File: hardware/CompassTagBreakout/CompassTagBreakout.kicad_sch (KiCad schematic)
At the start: 15 parts, among them J3 Conn_01x17, J4 Conn_01x17, U1 TPS7A2018PDQN, U2 AT25XE321, U3 AK09940A, U4 LIS2DU12TR

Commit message: checkpoint
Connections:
- net AK_MISO: now also U3.B4 (SO); no longer U3.A4 (SDA/SI)
- net AK_MOSI: now also U3.A4 (SDA/SI); no longer U3.B4 (SO)
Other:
- title: Tag Breakout Board Steval Dauguter -> Compass Tag Breakout
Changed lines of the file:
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@@
 	(paper "A")
 	(title_block
-		(title "Tag Breakout Board Steval Dauguter")
-		(date "2020-10-24")
+		(title "Compass Tag Breakout")
+		(date "2025-04-25")
 	)
 	(junction
@@
 		)
 	)
+	(label "AK_MOSI"
+		(at 140.97 86.36 180)
+		(effects
+			(font
+				(size 1.524 1.524)
+			)
+			(justify right bottom)
+		)
+	)
 	(label "AK_MISO"
-		(at 140.97 86.36 180)
-		(effects
-			(font
-				(size 1.524 1.524)
-			)
-			(justify right bottom)
-		)
-	)
-	(label "AK_MOSI"
 		(at 199.39 91.44 0)
 		(effects

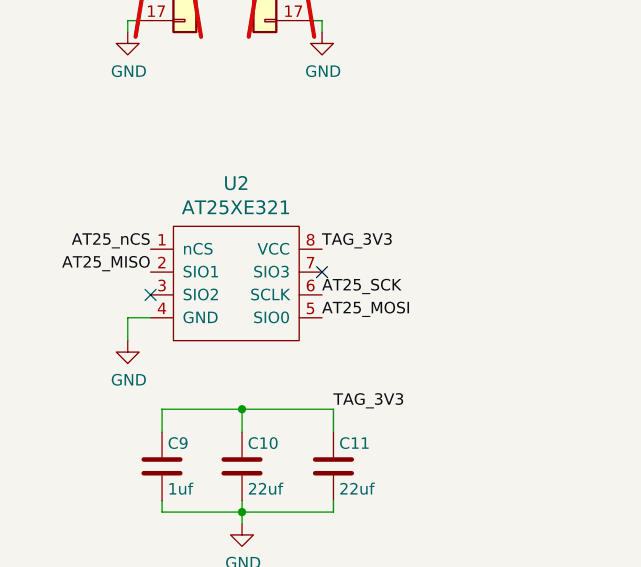
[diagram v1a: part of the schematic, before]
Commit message: checkpoint -- order compass proto board
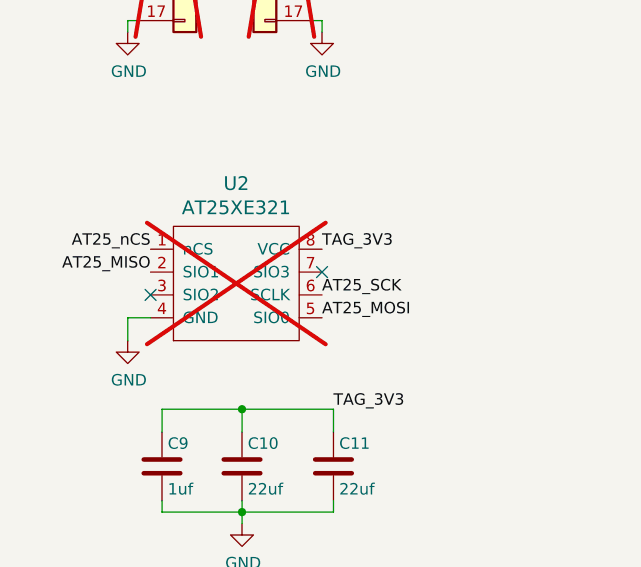
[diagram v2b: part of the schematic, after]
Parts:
- U2: now not fitted
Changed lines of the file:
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@@
 		(in_bom yes)
 		(on_board yes)
-		(dnp no)
+		(dnp yes)
 		(property "Reference" "U2"
 			(at 48.895 115.9002 0)
